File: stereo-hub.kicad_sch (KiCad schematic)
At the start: 61 parts, among them J1 Raspberry_Pi_2_3, J2 USB_C_Receptacle_USB2.0_14P, K2 Relay_SPDT, Q1 DMN10H220L, Q2 CSD17577Q3A, Q3 DMN10H220L, Q4 CSD17577Q3A, U1 STM32G0C1RCTx, U2 TLIN1029A-Q1, U3 MCP2542FDxMF, U4 TCPP02-M18, U5 ECMF02-2AMX6, U6 LMR33640DDDA, U7 CAT24C128

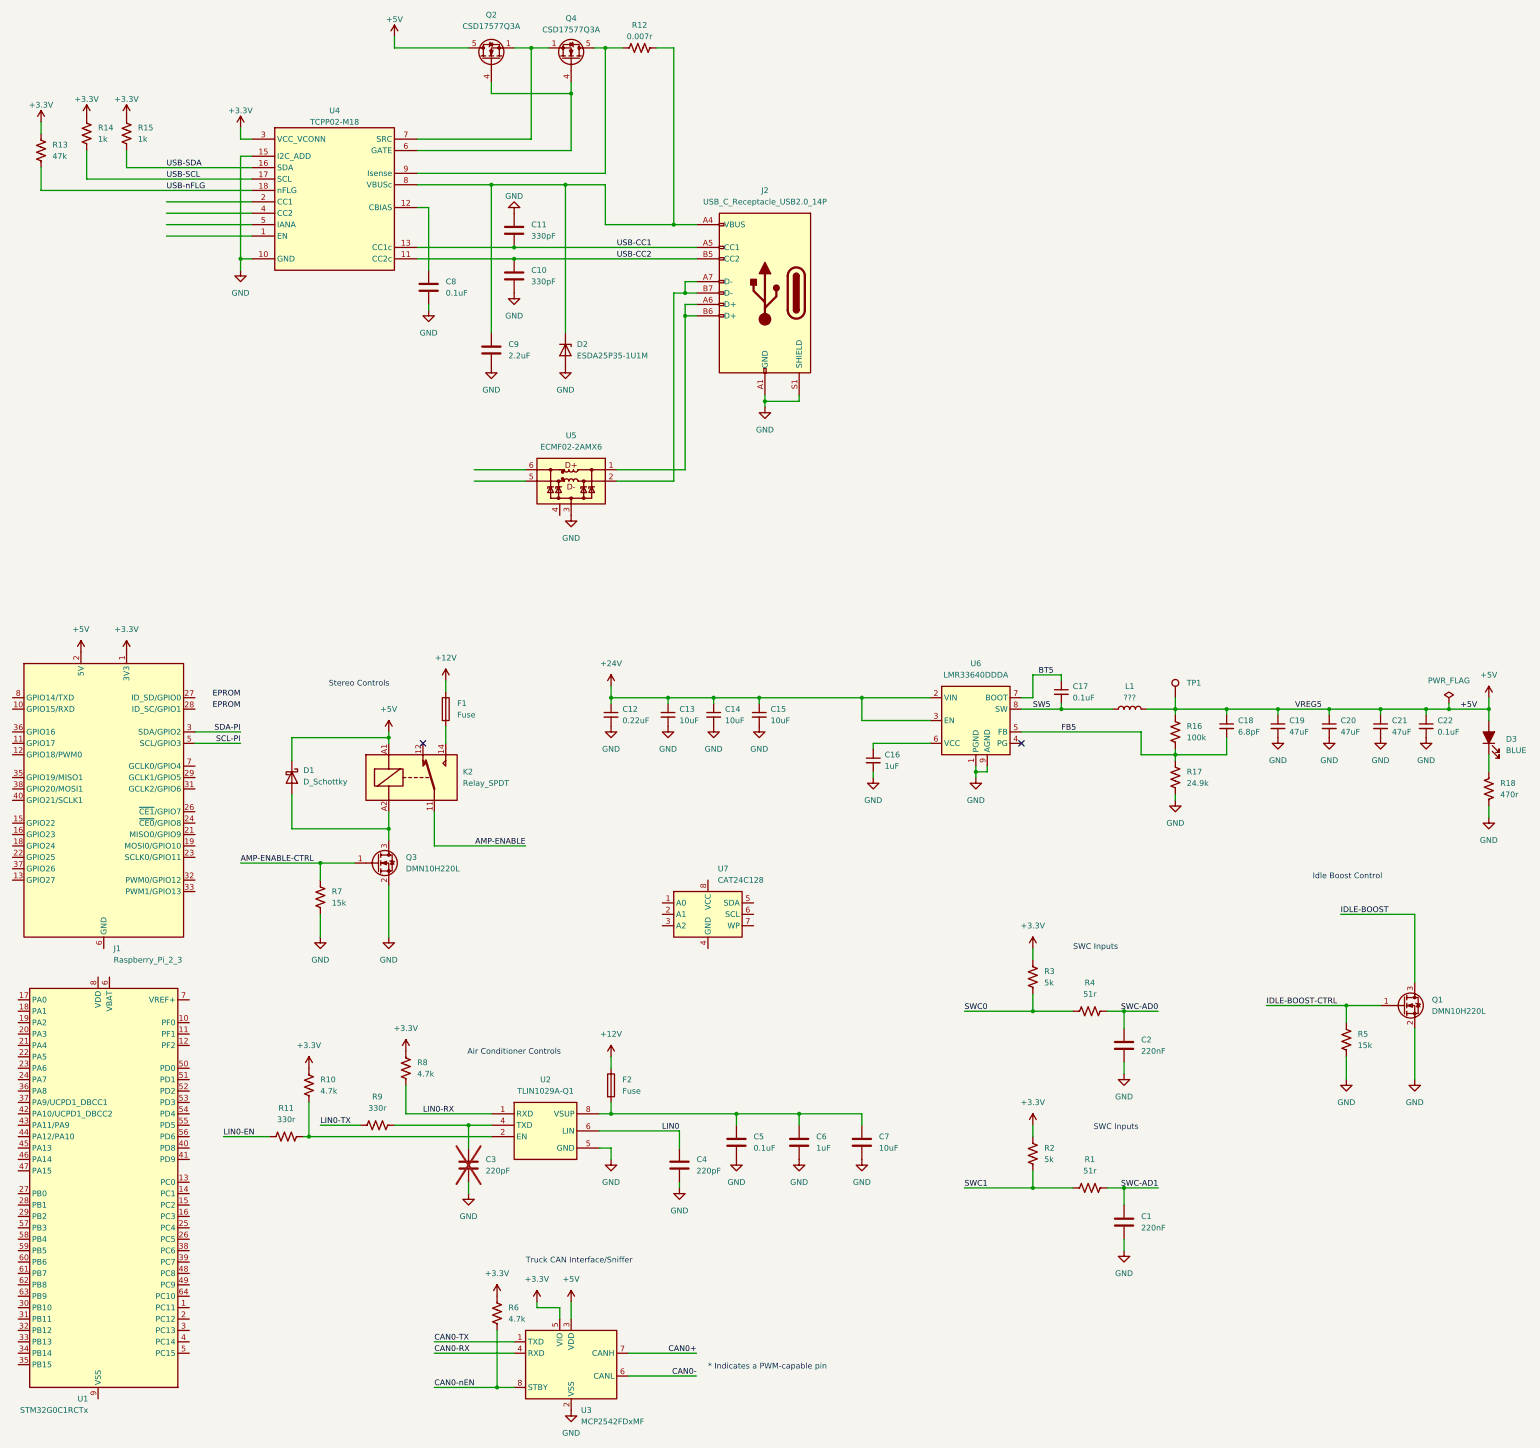
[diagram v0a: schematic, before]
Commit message: Start breaking up schematic into sheets
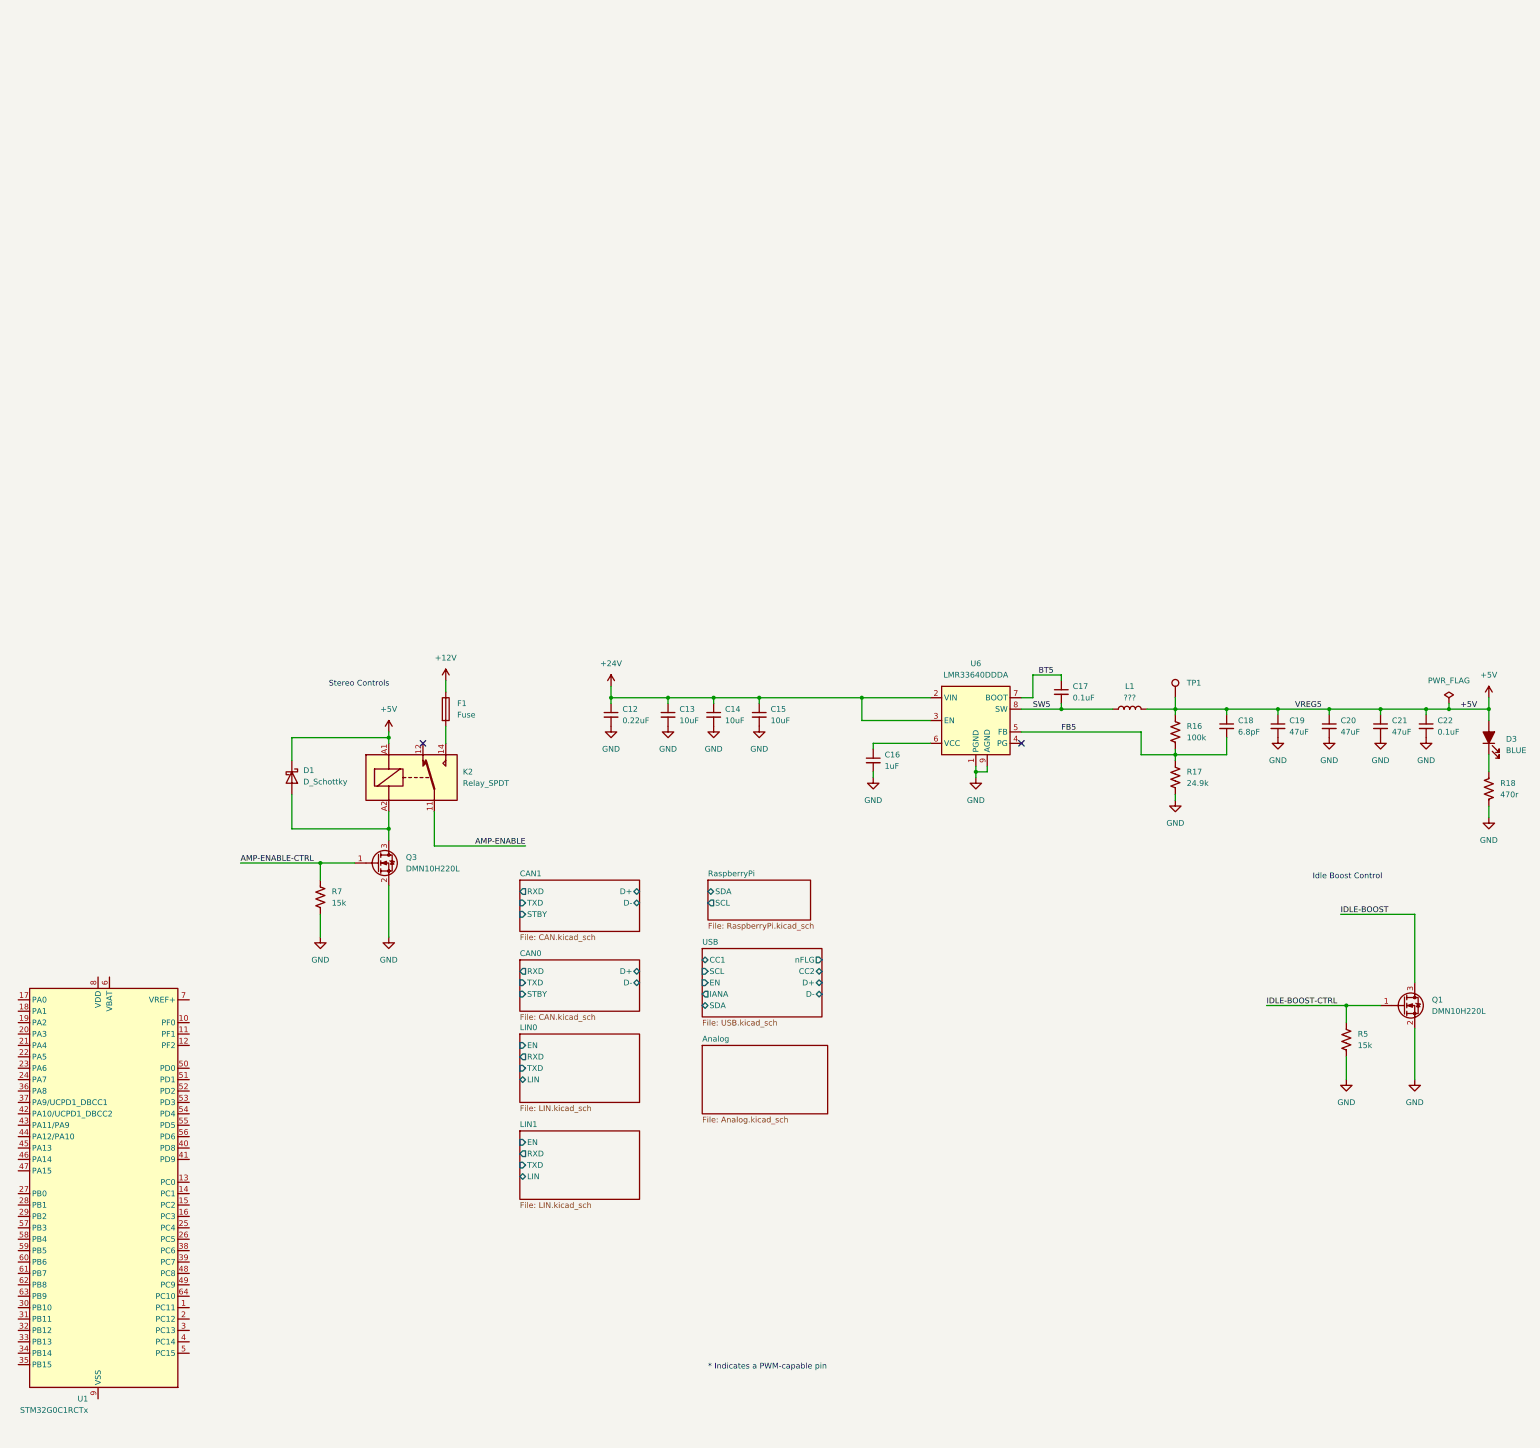
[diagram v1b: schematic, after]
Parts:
- removed C1, C2: 220nF, symbol Device:C
- removed C10, C11: 330pF, symbol Device:C
- removed C3, C4: 220pF, symbol Device:C
- removed C5, C8: 0.1uF, symbol Device:C
- removed C6: 1uF, symbol Device:C
- removed C7: 10uF, symbol Device:C
- removed C9: 2.2uF, symbol Device:C
- removed D2: ESDA25P35-1U1M, symbol Device:D_Zener
- removed F2: Fuse, symbol Device:Fuse
- removed J1: Raspberry_Pi_2_3, symbol Connector:Raspberry_Pi_2_3
- removed J2: USB_C_Receptacle_USB2.0_14P, symbol Connector:USB_C_Receptacle_USB2.0_14P
- removed Q2, Q4: CSD17577Q3A, Package_SON:VSON-8_3.3x3.3mm_P0.65mm_NexFET, symbol Transistor_FET:CSD17577Q3A
- removed R1, R4: 51r, symbol Device:R_US
- removed R10, R6, R8: 4.7k, symbol Device:R_US
- removed R11, R9: 330r, symbol Device:R_US
- removed R12: 0.007r, symbol Device:R_US
- removed R13: 47k, symbol Device:R_US
- removed R14, R15: 1k, symbol Device:R_US
- removed R2, R3: 5k, symbol Device:R_US
- removed U2: TLIN1029A-Q1, Package_SO:SOIC-8_3.9x4.9mm_P1.27mm, symbol steezeman:TLIN1029A-Q1
- removed U3: MCP2542FDxMF, Package_DFN_QFN:DFN-8-1EP_3x3mm_P0.65mm_EP1.55x2.4mm, symbol Interface_CAN_LIN:MCP2542FDxMF
- removed U4: TCPP02-M18, steezeman:QFN-18L_3P5X3P5_STM, symbol steezeman:TCPP02-M18
- removed U5: ECMF02-2AMX6, Package_DFN_QFN:ST_UQFN-6L_1.5x1.7mm_P0.5mm, symbol Power_Protection:ECMF02-2AMX6
- removed U7: CAT24C128, symbol Memory_EEPROM:CAT24C128
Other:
- added sheet Analog (Analog.kicad_sch)
- added sheet CAN0 (CAN.kicad_sch)
- added sheet CAN1 (CAN.kicad_sch)
- added sheet LIN0 (LIN.kicad_sch)
- added sheet LIN1 (LIN.kicad_sch)
- added sheet RaspberryPi (RaspberryPi.kicad_sch)
- added sheet USB (USB.kicad_sch)
- note removed: "Air Conditioner Controls"
- note removed: "SWC Inputs"
- note removed: "Truck CAN Interface/Sniffer"

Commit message: Updated with recent progress on schematic capture
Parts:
- removed C12: 0.22uF, Capacitor_SMD:C_0603_1608Metric, symbol Device:C_Small
- removed C13, C14, C15: 10uF, Capacitor_SMD:C_1206_3216Metric, symbol Device:C_Small
- removed C16: 1uF, Capacitor_SMD:C_0603_1608Metric, symbol Device:C_Small
- removed C17, C22: 0.1uF, Capacitor_SMD:C_0603_1608Metric, symbol Device:C_Small
- removed C18: 6.8pF, Capacitor_SMD:C_0603_1608Metric, symbol Device:C_Small
- removed C19, C20, C21: 47uF, Capacitor_SMD:C_2220_5650Metric, symbol Device:C_Small
- removed D1: D_Schottky, symbol Device:D_Schottky
- removed D3: BLUE, LED_SMD:LED_0603_1608Metric, symbol Device:LED_Filled
- removed F1: Fuse, symbol Device:Fuse
- removed K2: Relay_SPDT, symbol Relay:Relay_SPDT
- removed L1: ???, Inductor_SMD:L_Coilcraft_XAL6060-XXX, symbol Device:L
- removed Q1, Q3: DMN10H220L, Package_TO_SOT_SMD:SOT-23, symbol Transistor_FET:DMN10H220L
- removed R16: 100k, Resistor_SMD:R_0603_1608Metric, symbol Device:R_US
- removed R17: 24.9k, Resistor_SMD:R_0603_1608Metric, symbol Device:R_US
- removed R18: 470r, Resistor_SMD:R_0603_1608Metric, symbol Device:R_US
- removed R5, R7: 15k, symbol Device:R_US
- removed TP1: TP, TestPoint:TestPoint_THTPad_1.5x1.5mm_Drill0.7mm, symbol Connector:TestPoint
- removed U1: STM32G0C1RCTx, Package_QFP:LQFP-64_10x10mm_P0.5mm, symbol MCU_ST_STM32G0:STM32G0C1RCTx
- removed U6: LMR33640DDDA, Package_SO:Texas_HSOP-8-1EP_3.9x4.9mm_P1.27mm_ThermalVias, symbol Regulator_Switching:LMR33640DDDA
- added F10, F11, F7, F8, F9: 1A, symbol Device:Fuse
- added J10, J9: Screw_Terminal_01x08, symbol Connector:Screw_Terminal_01x08
- added R27: 120r, symbol Device:R_US
- added U4: TPSM53604RDA, Package_DFN_QFN:Texas_B3QFN-14-1EP_5x5.5mm_P0.65mm_ThermalVia, symbol Converter_DCDC:TPSM53604RDA
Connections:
- net +12V: now also F10.2, F7.2, F8.2, F9.2
- net +5V: now also U4.7 (VOUT), U4.8 (VOUT)
- net GND: now also J9.1 (Pin_1), J9.8 (Pin_8)
- new net: F11.2, R27.2
- new net: U4.1 (VIN), U4.14 (VIN)
- new net: U4.10 (PGND), U4.11 (PGND), U4.15 (PGND), U4.3 (PGND)
- new net ACC: J9.5 (Pin_5)
- new net COOL: J10.2 (Pin_2)
- new net HIGH-IDLE: F11.1, J10.1 (Pin_1)
- new net HOUSE: J9.2 (Pin_2)
- new net IGN: J9.4 (Pin_4)
- new net LIN: J10.3 (Pin_3)
- new net OD-0/LOW0: R27.1
- new net START: J9.3 (Pin_3)
- new net SWC0: J9.6 (Pin_6)
- new net SWC1: J9.7 (Pin_7)
- new net relay0/COM: F8.1
- new net relay1/COM: F7.1
- new net relay2/COM: F10.1
- new net relay3/COM: F9.1
- no-connect marks 2 -> 3
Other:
- sheet Analog renamed Analog0
- removed sheet CAN1
- removed sheet LIN1
- removed sheet RaspberryPi
- removed sheet USB
- added sheet OD-0 (open-drain.kicad_sch)
- added sheet OD-1 (open-drain.kicad_sch)
- added sheet OD-2 (open-drain.kicad_sch)
- added sheet OD-3 (open-drain.kicad_sch)
- added sheet OD-4 (open-drain.kicad_sch)
- added sheet OD-5 (open-drain.kicad_sch)
- added sheet mcu (mcu.kicad_sch)
- added sheet opto (opto.kicad_sch)
- added sheet relay0 (relay.kicad_sch)
- added sheet relay1 (relay.kicad_sch)
- added sheet relay2 (relay.kicad_sch)
- added sheet relay3 (relay.kicad_sch)
- added sheet remote-starter (remote-starter.kicad_sch)
- added sheet rpi (rpi.kicad_sch)
- added sheet sense (sense.kicad_sch)
- sheet Analog0 ports: added ADC0, ADC1, IN0, IN1; removed none
- sheet CAN0 ports: added none; removed D+, D-, STBY
- note added: "CHASSIS"
- note added: "SWCC"
- note removed: "* Indicates a PWM-capable pin"
- note removed: "Idle Boost Control"
- note removed: "Stereo Controls"
